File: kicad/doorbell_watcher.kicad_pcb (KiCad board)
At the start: 2 copper layers, 45 x 66 mm, 26 parts, among them J1 Screw Terminal, J2 Conn_01x10, J3 Conn_01x10, J4 Conn_01x10, U1 ACPL-214-500E, U2 LM2596S-5

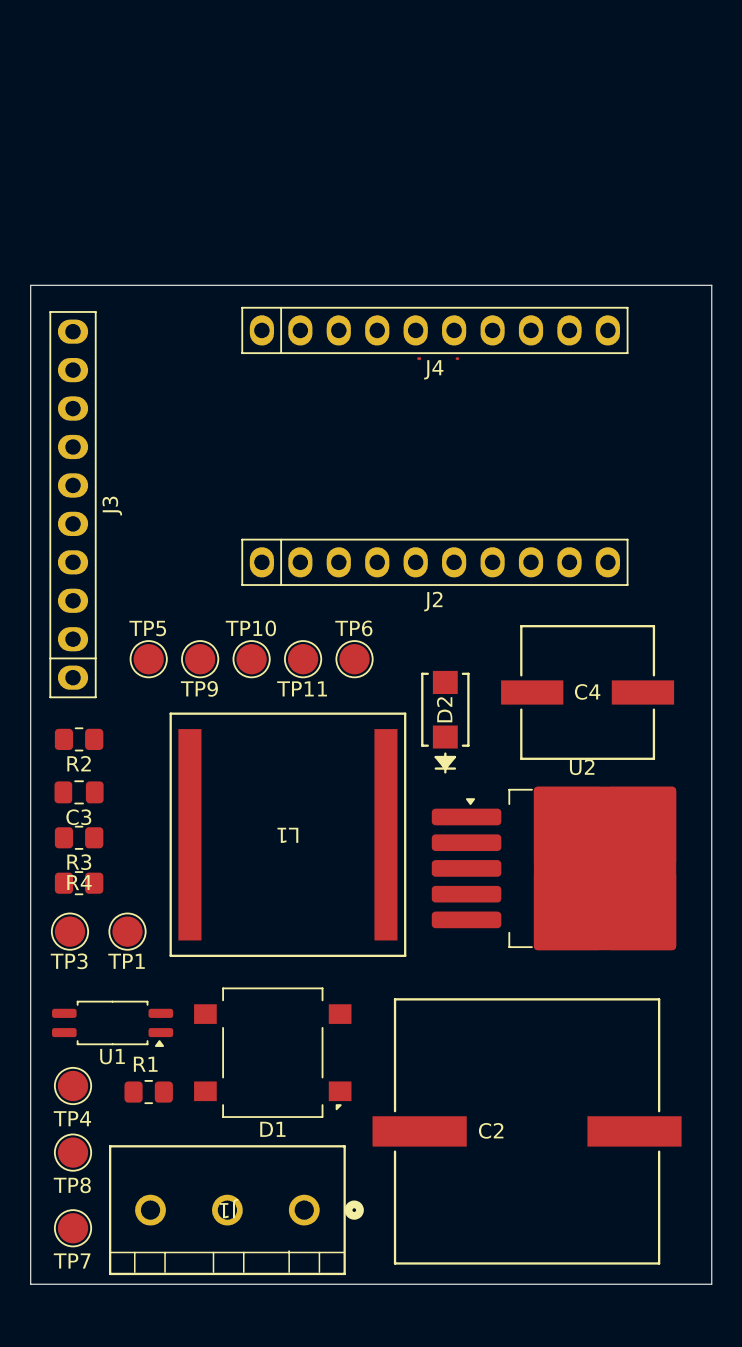
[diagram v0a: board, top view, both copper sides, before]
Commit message: Routing complete, changed LM2596 to LM2594
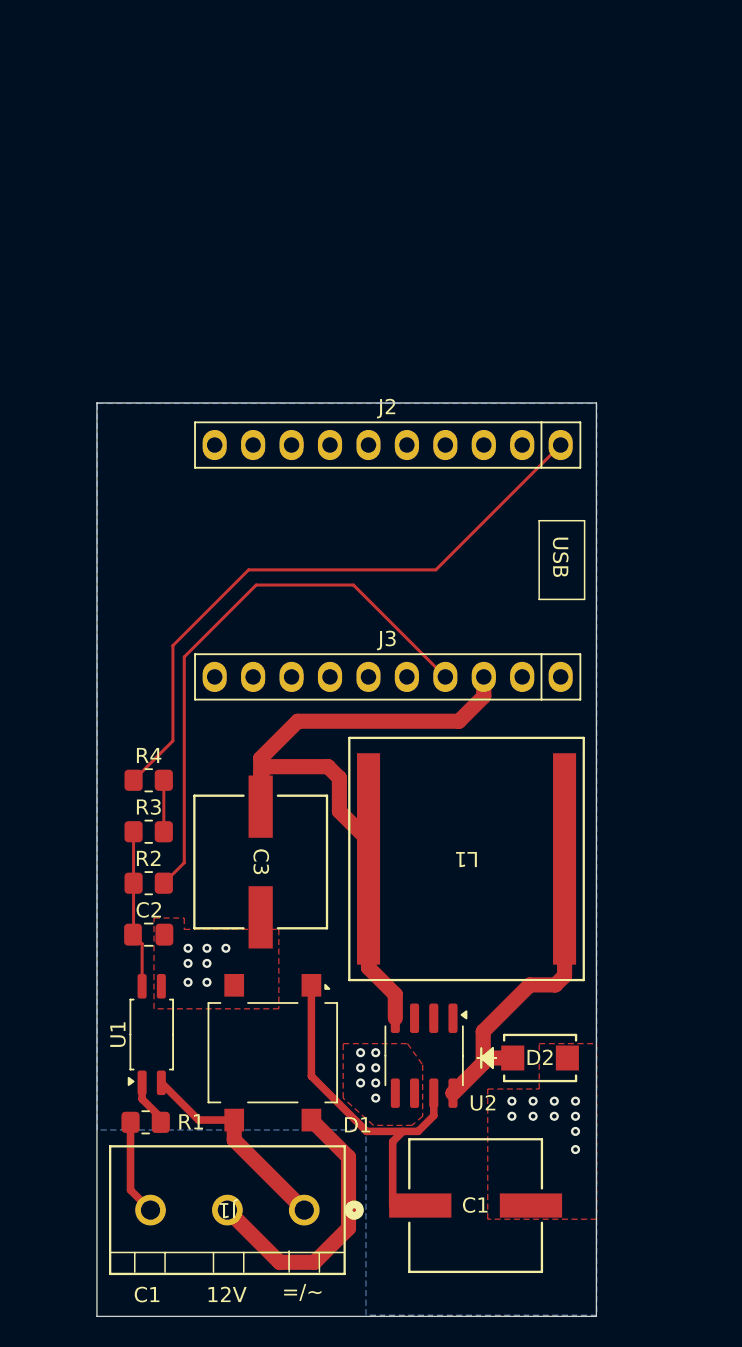
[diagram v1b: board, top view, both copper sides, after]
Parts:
- removed the C2 at (144.4, 109.6)
- removed the J3 at (114.4, 68.2)
- removed TP1, TP10, TP11, TP3, TP4, TP5, TP6, TP7, TP8, TP9: ~, TestPoint:TestPoint_Pad_D2.0mm
- added C1: 220u, parts_lib:CAP_EEFK_F_PAN-M, F.Cu at (141.0, 114.5)
- U2: value LM2596S-5 -> LM2594M-5.0; footprint Package_TO_SOT_SMD:TO-263-5_TabPin3 -> Package_SO:SOIC-8_3.9x4.9mm_P1.27mm
- moved C3 24.3 mm to (126.8, 91.8), turned to -90 degrees
- moved D2 23.8 mm to (145.3, 104.8), turned to 0 degrees
- moved J3 23.1 mm to (135.2, 79.6), turned to 180 degrees
- moved U2 16.2 mm to (137.6, 104.6), turned to -90 degrees
- moved L1 11.9 mm to (140.4, 91.6)
- moved R2 10.6 mm to (119.4, 93.2), turned to 0 degrees
- moved C2 10.5 mm to (119.4, 96.6), turned to 0 degrees
- moved J2 8.35 mm to (135.2, 64.2), turned to 180 degrees
- moved R4 8.21 mm to (119.4, 86.4)
- moved R3 4.62 mm to (119.4, 89.8), turned to 0 degrees
- moved U1 2.70 mm to (119.6, 103.2), turned to 90 degrees
- moved R1 2.01 mm to (119.2, 109.0)
- turned D1 to -90 degrees
- renumbered C3 to C2, C4 to C3, J4 to J3
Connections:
- J3 pad 10: /IO25 -> unconnected-(J3-Pin_10-Pad10)
- J3 pad 7: /IO15 -> unconnected-(J3-Pin_7-Pad7)
- J3 pad 8: /IO27 -> unconnected-(J3-Pin_8-Pad8)
- J3 pad 9: /IO26 -> unconnected-(J3-Pin_9-Pad9)
- U2 pad 1: Net-(D1-+) -> unconnected-(U2-NC-Pad1)
- U2 pad 2: Net-(D2-K) -> unconnected-(U2-NC-Pad2)
- U2 pad 3: GND -> unconnected-(U2-NC-Pad3)
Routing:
- net +5V: track 0.08 -> 49.9 mm
- net /IO23: track 0.00 -> 41.8 mm
- net +3V3: track 0.04 -> 37.2 mm
- net Net-(D2-K): track 0.00 -> 25.1 mm
- net Net-(D1-+): track 0.00 -> 24.5 mm
- net /Vin2: track 0.00 -> 18.5 mm
- net /Vin1: track 0.00 -> 13.7 mm
- net Net-(C2-Pad1): track 0.11 -> 10.5 mm
- net /C1: track 0.00 -> 6.35 mm
- net /ButtonPressed: track 0.00 -> 3.40 mm
- net Net-(R1-Pad2): track 0.00 -> 3.12 mm
- net GND: vias 0 -> 24
- added copper zone on B.Cu, net GND
- added copper zone on F.Cu, net GND
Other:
- board size 45 x 66 mm -> 33 x 60.4 mm
- board text added: "12V"
- board text added: "=/~"
- board text added: "C1"
- board text added: "USB"

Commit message: Added fabrication files
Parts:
- added FD1: Fiducial_0.5mm_Mask1mm, Fiducial:Fiducial_0.5mm_Mask1mm, F.Cu at (117.6, 63.0)
- added FD1: Fiducial_0.5mm_Mask1mm, Fiducial:Fiducial_0.5mm_Mask1mm, F.Cu at (147.4, 120.2)

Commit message: First fabrication release done
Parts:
- removed the FD1 at (117.6, 63.0)
- removed the FD1 at (147.4, 120.2)
- added FD1: Fiducial_0.5mm_Mask1mm, Fiducial:Fiducial_0.5mm_Mask1mm, F.Cu at (118.0, 63.2)
- added FD2: Fiducial_0.5mm_Mask1mm, Fiducial:Fiducial_0.5mm_Mask1mm, F.Cu at (147.2, 120.4)
- C1, C3: footprint parts_lib:CAP_EEFK_F_PAN-M -> parts_lib:CAP_FT_F_PAN-M
- D1: value DF01S1 -> MDB10S
- J1: value Screw Terminal -> Screw Terminal 01x03
- U2: value LM2594M-5.0 -> LM2594MX-5.0
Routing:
- net +5V: track 49.9 -> 15.0 mm
- added copper zone on F.Cu, net +5V
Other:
- board text added: "pingring.me"

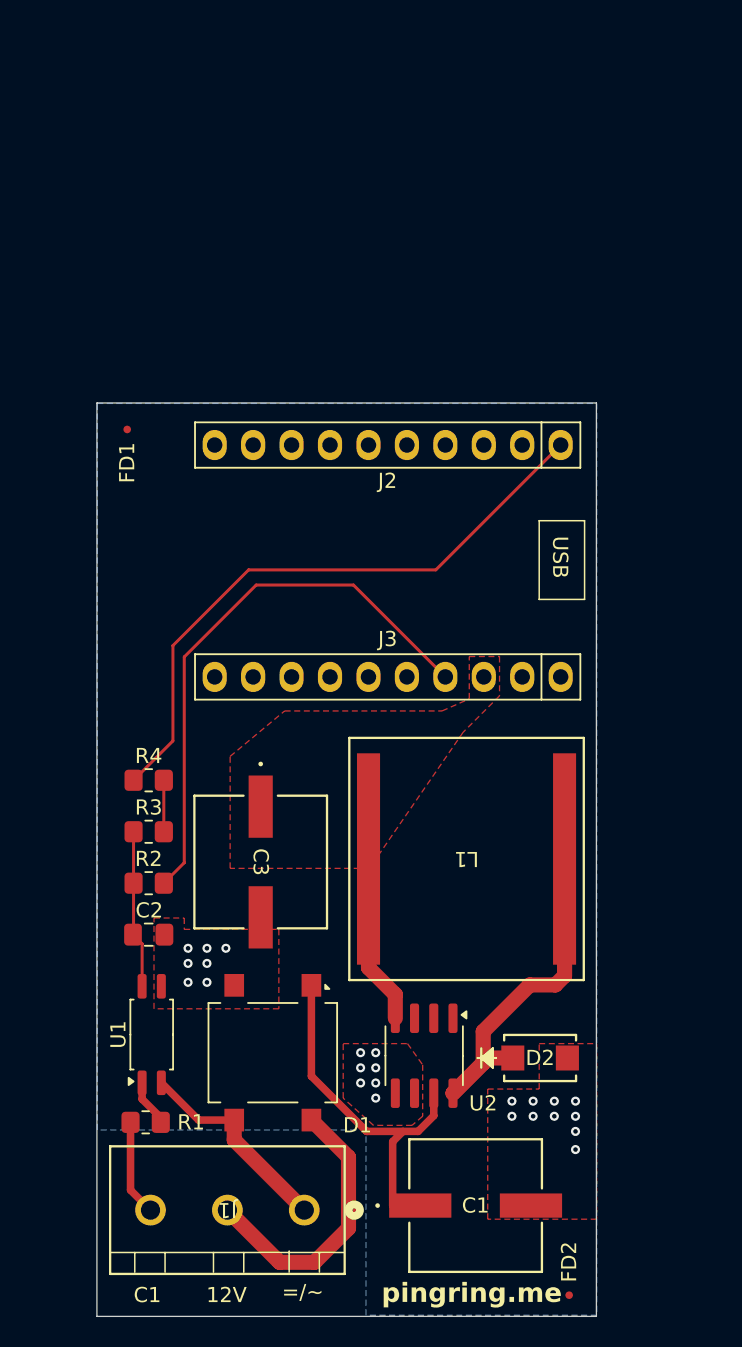
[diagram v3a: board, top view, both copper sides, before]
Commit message: Fix MDB9S footprint
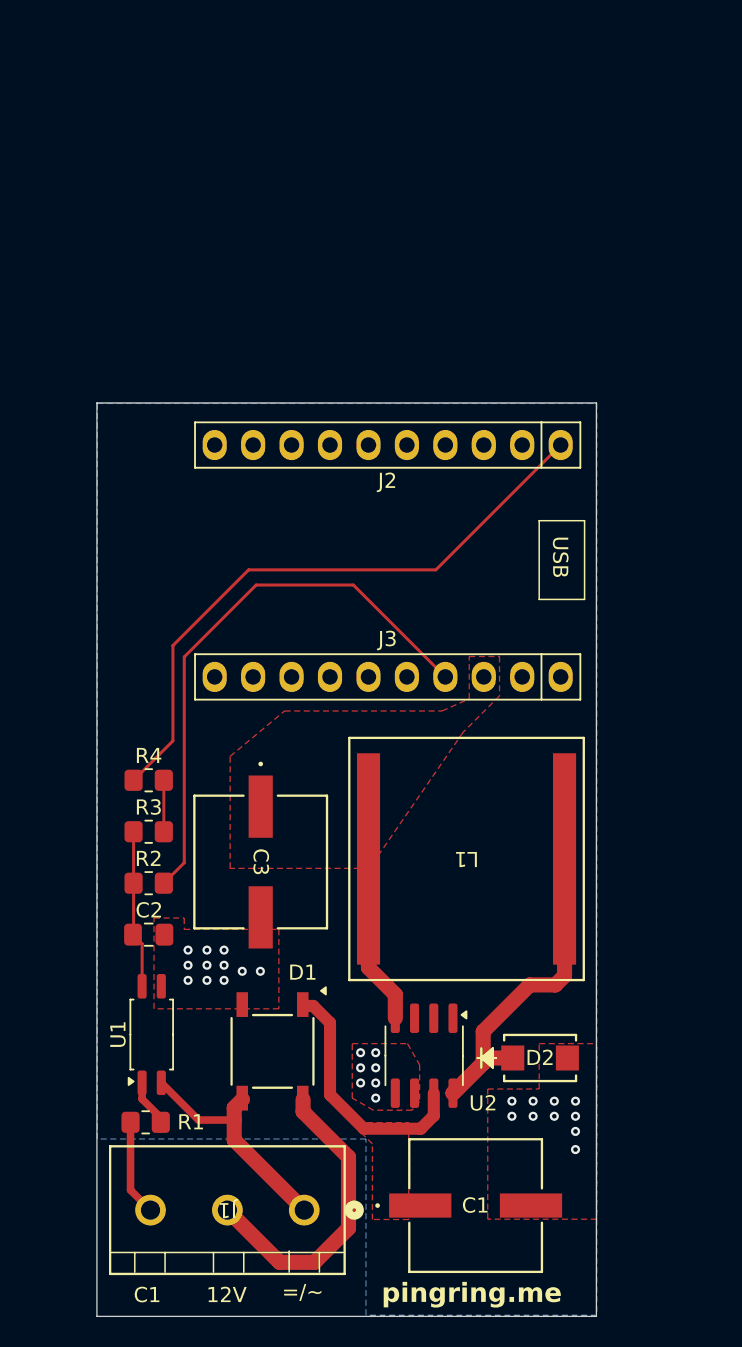
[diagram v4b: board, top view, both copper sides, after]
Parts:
- removed FD1, FD2: Fiducial_0.5mm_Mask1mm, Fiducial:Fiducial_0.5mm_Mask1mm
- D1: footprint Diode_SMD:Diode_Bridge_OnSemi_SDIP-4L -> parts_lib:TSSOP4-MICRO-DIP_948BS_ONS-M
- moved D1 0.09 mm to (127.6, 104.3)
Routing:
- net Net-(D1-+): track 24.5 -> 16.6 mm
- net /Vin2: track 18.5 -> 20.1 mm
- net /Vin1: track 13.7 -> 15.3 mm
- net GND: vias 24 -> 28
- added copper zone on F.Cu, net Net-(D1-+)

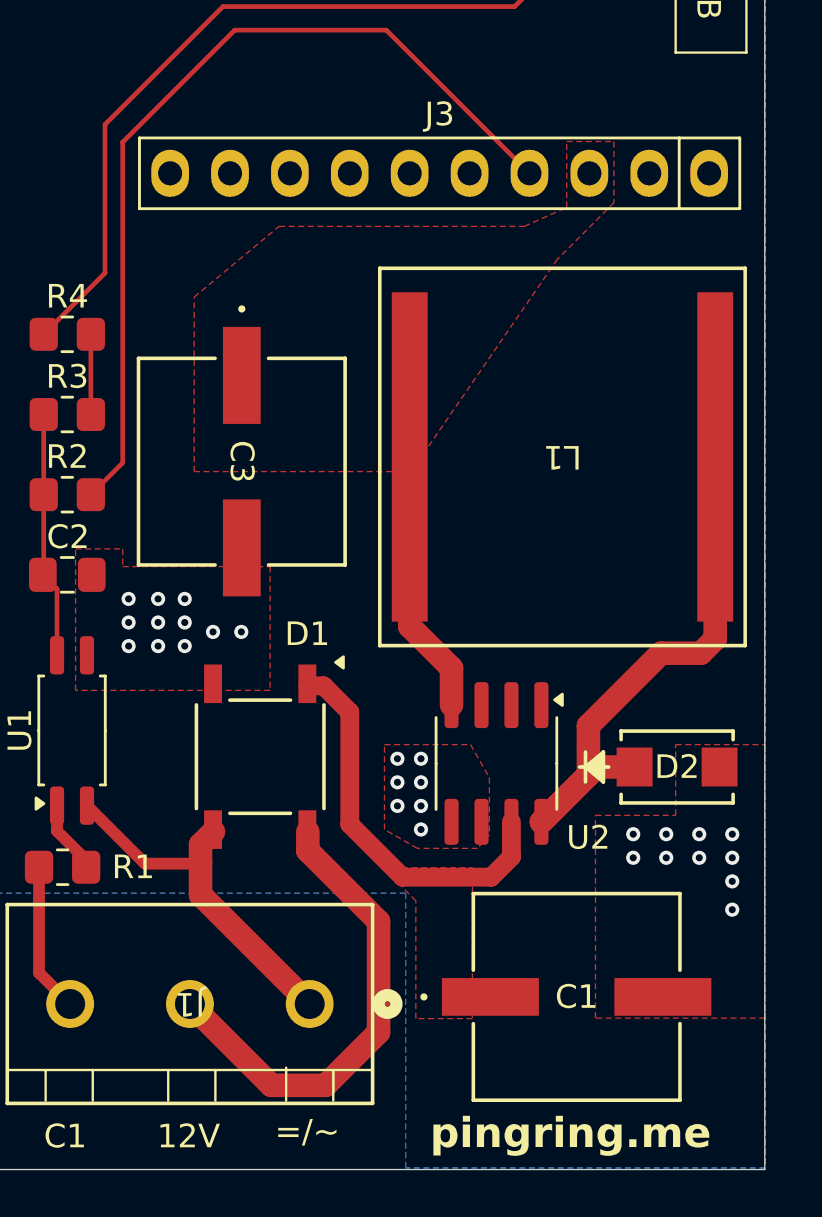
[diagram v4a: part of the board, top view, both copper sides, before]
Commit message: Fix unconnected 5V pin in ESP32 header
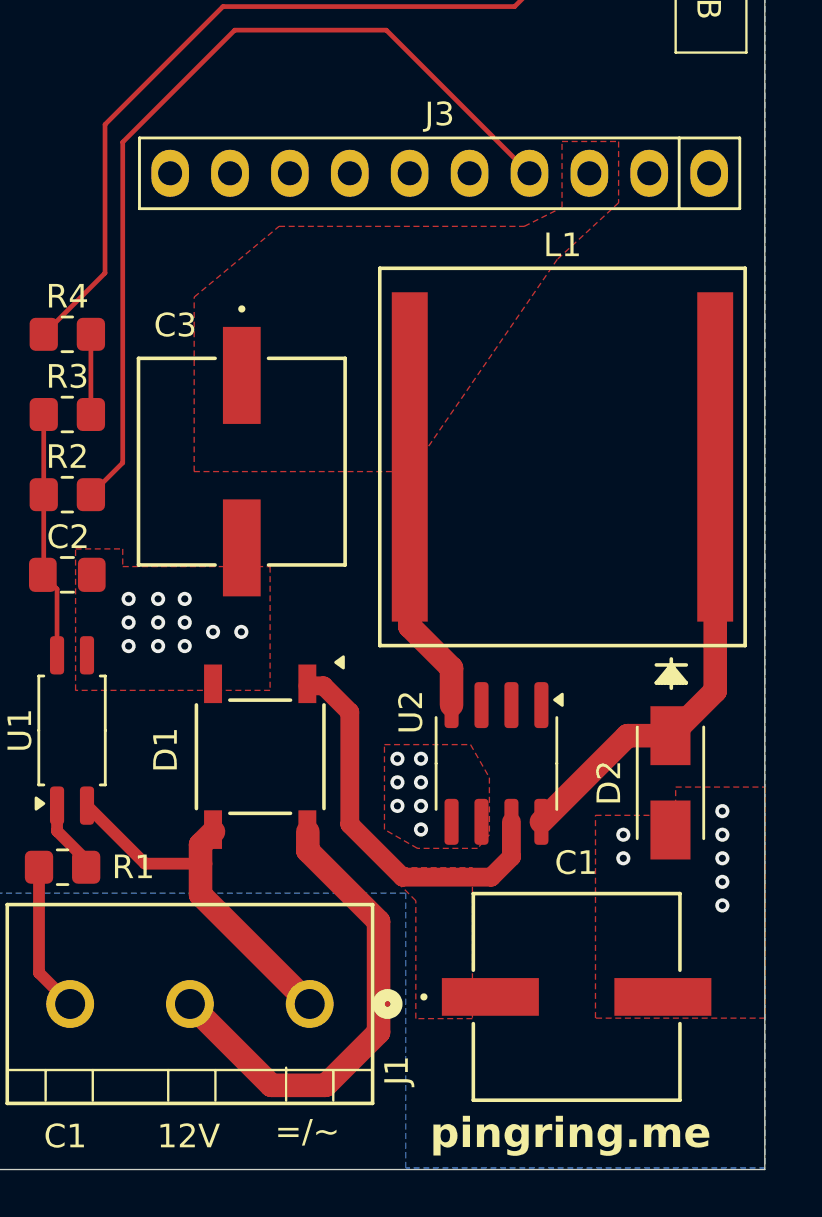
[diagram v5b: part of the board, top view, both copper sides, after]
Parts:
- D2: footprint parts_lib:ss24_do214AC -> parts_lib:DO-214AC(SMA)
- moved D2 0.73 mm to (145.0, 105.4), turned to -90 degrees
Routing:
- net Net-(D2-K): track 25.1 -> 19.6 mm
- net GND: vias 28 -> 25

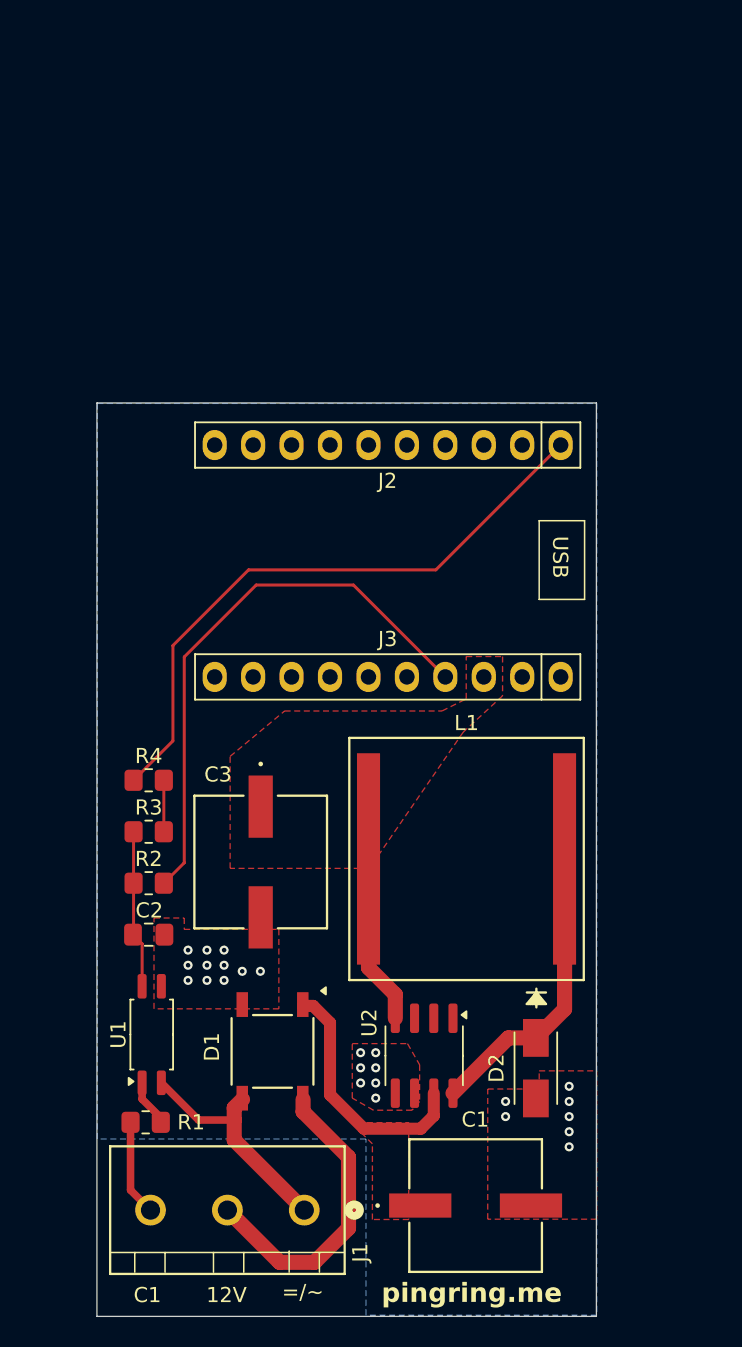
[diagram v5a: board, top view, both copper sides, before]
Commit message: Add relay
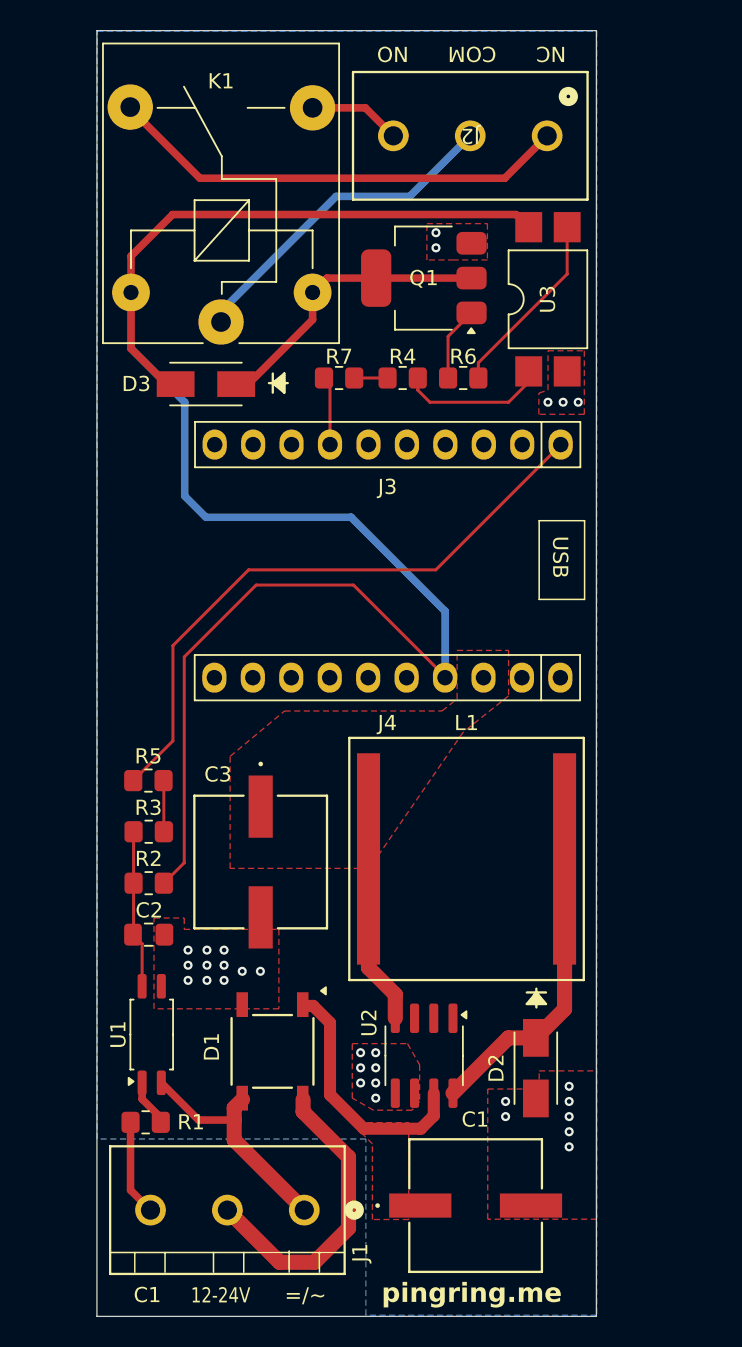
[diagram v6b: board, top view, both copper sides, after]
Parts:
- added D3: SS24, parts_lib:DO-214AC(SMA), F.Cu at (123.2, 60.2)
- added J4: Conn_01x10, parts_lib:10-pin header, F.Cu at (135.2, 79.6)
- added K1: SANYOU_SRD_Form_C, Relay_THT:Relay_SPDT_SANYOU_SRD_Series_Form_C, F.Cu at (124.2, 56.1)
- added Q1: PZT2222A, Package_TO_SOT_SMD:SOT-223-3_TabPin2, F.Cu at (137.6, 53.2)
- added R5: 0R, Resistor_SMD:R_0805_2012Metric_Pad1.20x1.40mm_HandSolder, F.Cu at (119.4, 86.4)
- added R6: 1K, Resistor_SMD:R_0805_2012Metric_Pad1.20x1.40mm_HandSolder, F.Cu at (140.2, 59.8)
- added R7: 0R, Resistor_SMD:R_0805_2012Metric_Pad1.20x1.40mm_HandSolder, F.Cu at (132.0, 59.8)
- added U3: LTV-817S, Package_DIP:SMDIP-4_W9.53mm, F.Cu at (145.8, 54.6)
- J1: value Screw Terminal 01x03 -> Screw_Terminal_01x03
- J2: value Conn_01x10 -> Screw_Terminal_01x03; footprint parts_lib:10-pin header -> parts_lib:screw_connector_1x3
- R4: value 0R -> 100R
- moved R4 31.4 mm to (136.2, 59.8), turned to 0 degrees
- moved J2 23.0 mm to (145.7, 43.8)
- moved J3 15.3 mm to (135.2, 64.2)
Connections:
- net /C1 renamed /Sense1
- J2 pad 1: /IO23 -> /RelayNC
- J2 pad 2: /IO19 -> /RelayCOM
- J2 pad 3: /IO18 -> /RelayNO
- J3 pad 1: unconnected-(J3-Pin_1-Pad1) -> /IO23
- J3 pad 10: unconnected-(J3-Pin_10-Pad10) -> GND
- J3 pad 2: GND -> /IO19
- J3 pad 3: +5V -> /IO18
- J3 pad 4: +3V3 -> /IO5
- J3 pad 5: /IO4 -> /IO22
- J3 pad 6: /IO14 -> /IO21
- J3 pad 7: unconnected-(J3-Pin_7-Pad7) -> /IO32
- J3 pad 8: unconnected-(J3-Pin_8-Pad8) -> /IO33
- R4 pad 1: /ButtonPressed -> /EnableRelay
- R4 pad 2: /IO23 -> Net-(R4-Pad2)
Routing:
- net +3V3: track 37.2 -> 114.7 mm
- net /RelayNC: track 0.00 -> 30.7 mm
- net /RelayCOM: track 0.00 -> 22.0 mm
- net Net-(D3-A): track 0.00 -> 20.1 mm
- net Net-(R6-Pad1): track 0.00 -> 12.4 mm
- net Net-(R4-Pad2): track 0.00 -> 9.72 mm
- net /RelayNO: track 0.00 -> 6.10 mm
- net Net-(Q1-B): track 0.00 -> 4.94 mm
- net /IO32: track 0.00 -> 4.57 mm
- net /EnableRelay: track 0.00 -> 2.20 mm
- net GND: vias 25 -> 30
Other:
- board size 33 x 60.4 mm -> 33 x 84.9 mm
- board text added: "12-24V"
- board text added: "COM"
- board text added: "NC"
- board text added: "NO"
- board text removed: "12V"
